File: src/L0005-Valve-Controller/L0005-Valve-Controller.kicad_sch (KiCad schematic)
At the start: 33 parts, among them J1 Jumper_NO, P1 3220-20-0200-00, P14 647676-3, P15 647676-3, P16 647676-2, P2 140-504-415-000, P9 647676-2, U2 LMS8117AMP-3.3_NOPB, U5 Optocoupler

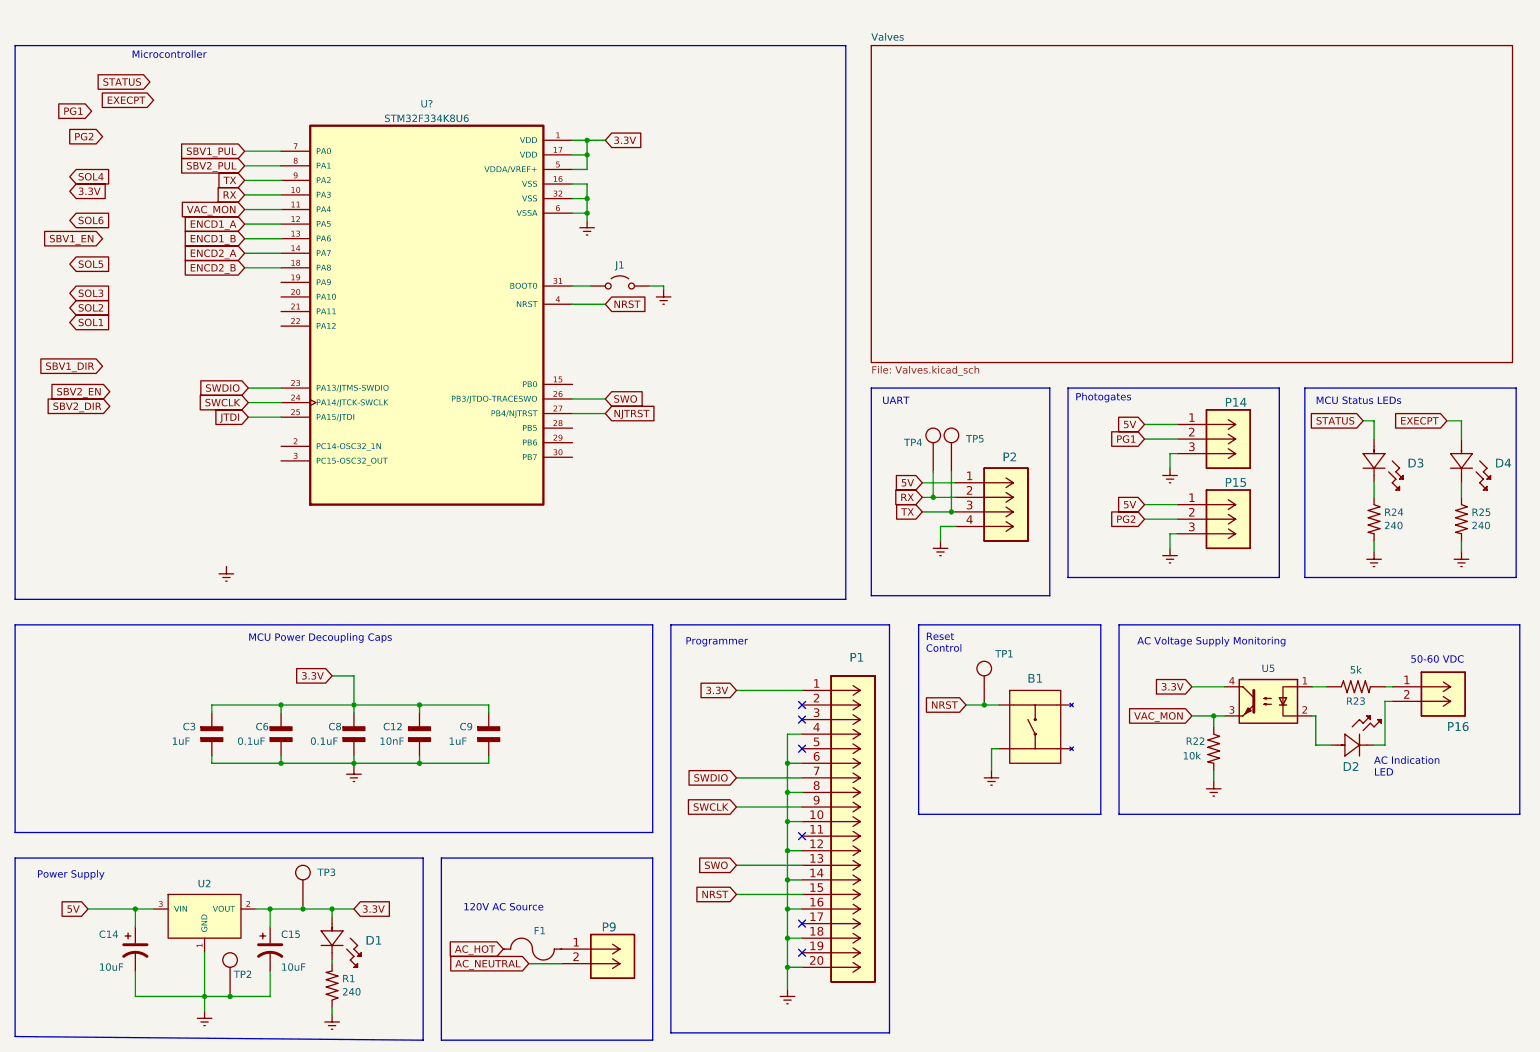
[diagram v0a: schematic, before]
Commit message: added solenoid control decoder
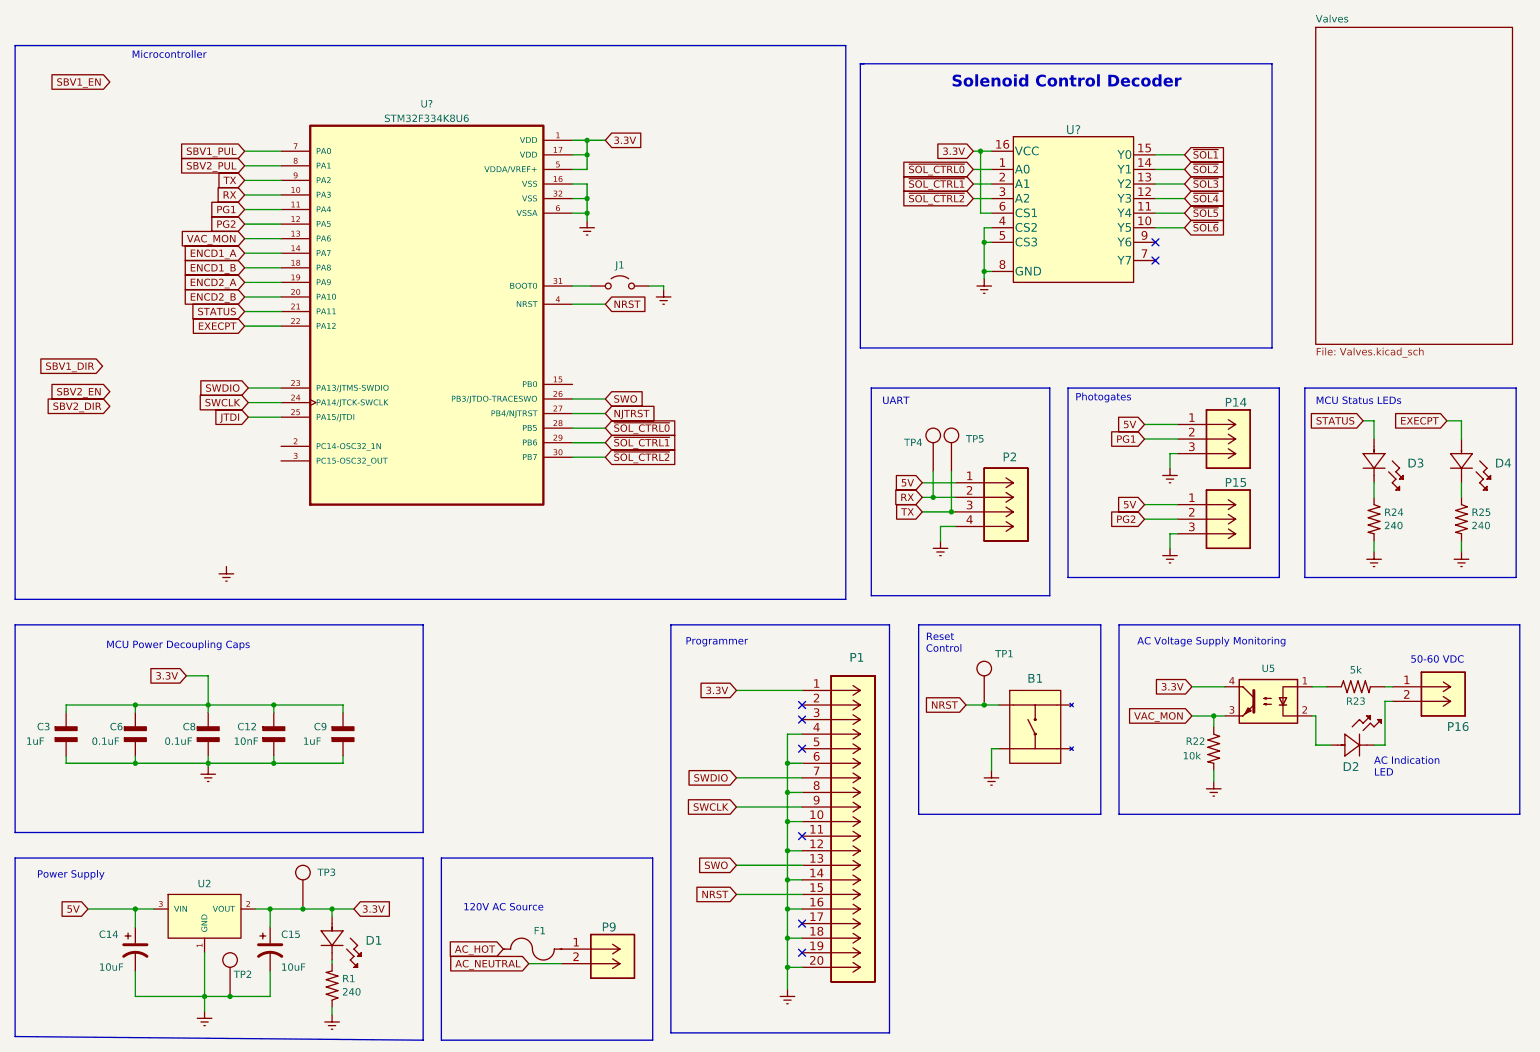
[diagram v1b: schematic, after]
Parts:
- added U?: MC74HCT138ADR2G, SOIC-16_ONS, symbol L0005-Valve-Controller:MC74HCT138ADR2G
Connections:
- net 3.3V: now also U?.16 (VCC), U?.6 (CS1)
- net ENCD1_A: now also U?.14 (PA7); no longer U?.12 (PA5)
- net ENCD1_B: now also U?.18 (PA8); no longer U?.13 (PA6)
- net ENCD2_A: now also U?.19 (PA9); no longer U?.14 (PA7)
- net ENCD2_B: now also U?.20 (PA10); no longer U?.18 (PA8)
- net EXECPT: now also U?.22 (PA12)
- net Earth: now also U?.4 (CS2), U?.5 (CS3), U?.8 (GND)
- net PG1: now also U?.11 (PA4)
- net PG2: now also U?.12 (PA5)
- net STATUS: now also U?.21 (PA11)
- net VAC_MON: now also U?.13 (PA6); no longer U?.11 (PA4)
- net ~{SOL_CTRL0}: now reaches U?.28 (PB5)
- net ~{SOL_CTRL0}: now also U?.1 (A0)
- net ~{SOL_CTRL1}: now reaches U?.29 (PB6)
- net ~{SOL_CTRL1}: now also U?.2 (A1)
- net ~{SOL_CTRL2}: now reaches U?.30 (PB7)
- net ~{SOL_CTRL2}: now also U?.3 (A2)
- new net ~{SOL1}: U?.15 (Y0)
- new net ~{SOL2}: U?.14 (Y1)
- new net ~{SOL3}: U?.13 (Y2)
- new net ~{SOL4}: U?.12 (Y3)
- new net ~{SOL5}: U?.11 (Y4)
- new net ~{SOL6}: U?.10 (Y5)
- no-connect marks 6 -> 8
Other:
- note added: "Solenoid Control Decoder"
- moved on the sheet: C12, C3, C6, C8, C9

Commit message: added STM32H7 MCU
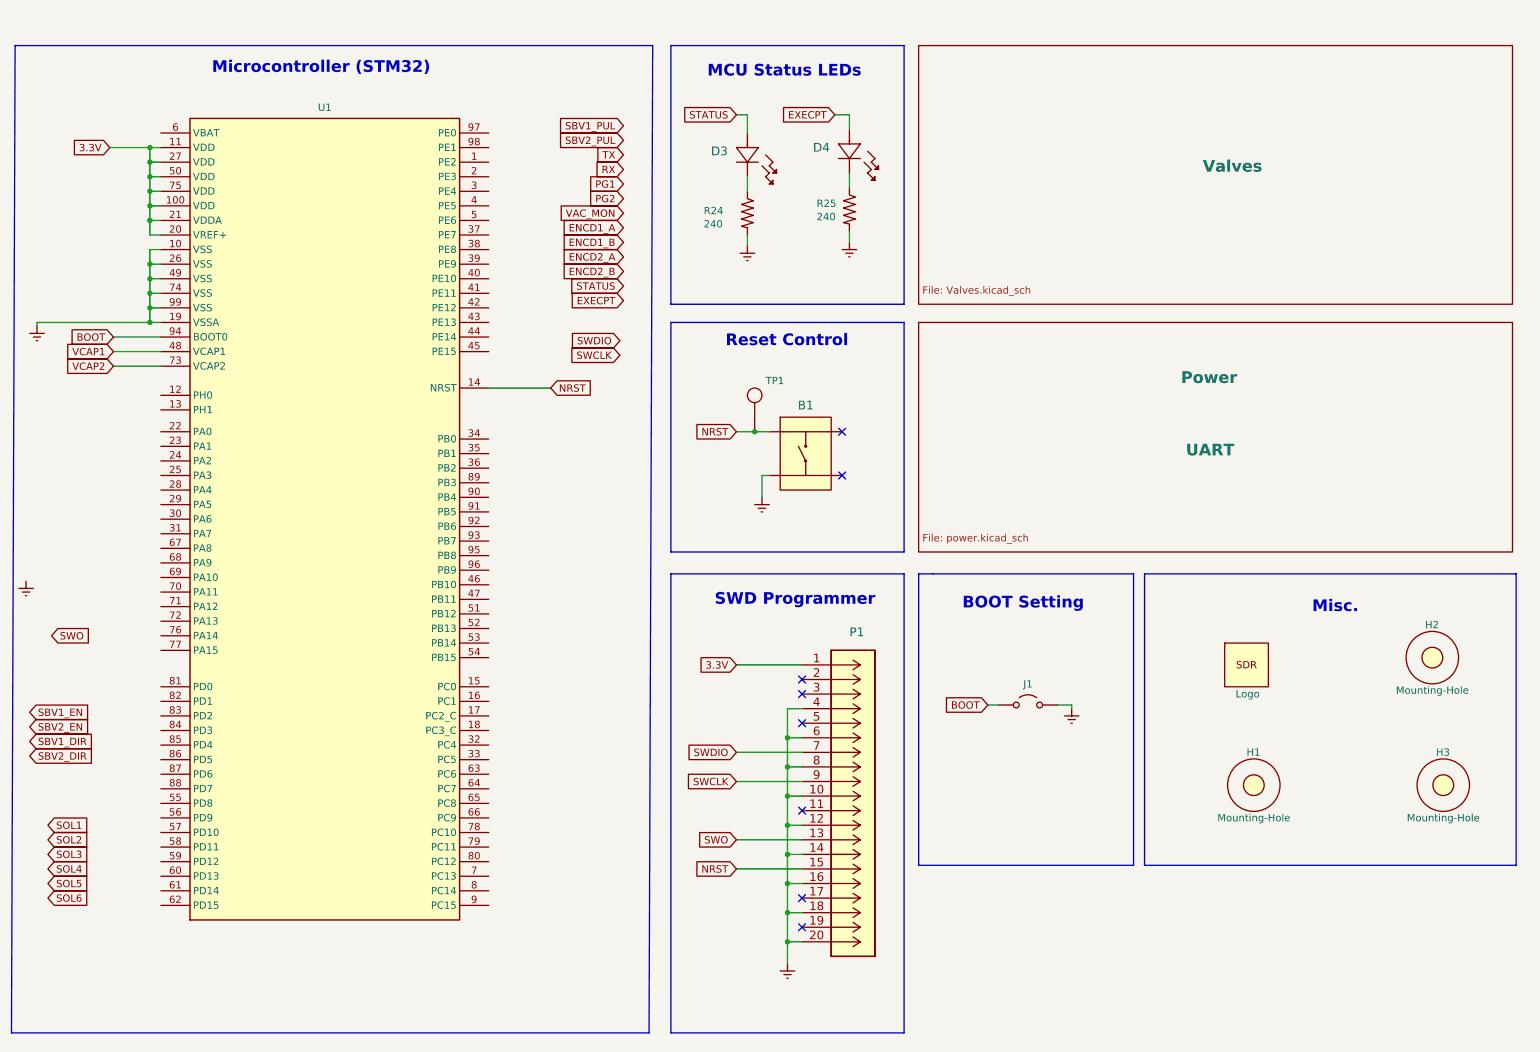
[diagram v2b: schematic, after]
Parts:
- removed C12: 10nF, L0005-Valve-Controller:CAP_0603, symbol L0005-Valve-Controller:CAP_0603
- removed C14, C15: 10uF, L0005-Valve-Controller:T491A106K010AT, symbol L0005-Valve-Controller:CAP_Polar
- removed C3, C9: 1uF, L0005-Valve-Controller:CAP_0603, symbol L0005-Valve-Controller:CAP_0603
- removed C6, C8: 0.1uF, L0005-Valve-Controller:CAP_0603, symbol L0005-Valve-Controller:CAP_0603
- removed D1, D2: LED_GREEN, L0005-Valve-Controller:SML-LX1206GC-TR, symbol L0005-Valve-Controller:LED_GREEN
- removed F1: 0678L9100-02, L0005-Valve-Controller:FUSC9830X318N, symbol L0005-Valve-Controller:0678L9100-02
- removed P14, P15: 647676-3, L0005-Valve-Controller:647676-3, symbol L0005-Valve-Controller:647676-3
- removed P16, P9: 647676-2, L0005-Valve-Controller:TE_647676-2, symbol L0005-Valve-Controller:647676-2
- removed P2: 140-504-415-000, L0005-Valve-Controller:140-504-415-000, symbol L0005-Valve-Controller:140-504-415-000
- removed R1: 240, L0005-Valve-Controller:RES_0603, symbol L0005-Valve-Controller:RES_0603
- removed R22: 10k, L0005-Valve-Controller:RES_0603, symbol L0005-Valve-Controller:RES_0603
- removed R23: 5k, L0005-Valve-Controller:RES_0603, symbol Engine-Controller:RES_0805
- removed TP2, TP3, TP4, TP5: TP, L0005-Valve-Controller:TP, symbol L0005-Valve-Controller:TP
- removed U2: LMS8117AMP-3.3_NOPB, L0005-Valve-Controller:LMS8117AMP-3.3NOPB, symbol L0005-Valve-Controller:LMS8117AMP-3.3_NOPB
- removed U5: Optocoupler, L0005-Valve-Controller:Opto_140105146000, symbol L0005-Valve-Controller:Optocoupler
- removed U?: MC74HCT138ADR2G, SOIC-16_ONS, symbol L0005-Valve-Controller:MC74HCT138ADR2G
- removed U?: STM32F334K8U6, QFN50P500X500X60-33N, symbol L0005-Valve-Controller:STM32F334K8U6
- added H1, H2, H3: Mounting-Hole, L0005-Valve-Controller:MountingHole_4.3mm_M4_DIN965, symbol L0005-Valve-Controller:Mounting-Hole
- added LOGO1: Logo, L0005-Valve-Controller:Logo, symbol L0005-Valve-Controller:Logo
- added U1: (no value), symbol L0005-Valve-Controller:STM32H750VBTx
- B1: value PTS647SM38SMTR2LFS -> (none); footprint L0005-Valve-Controller:PTS647SM38SMTR2LFS -> SW_PTS647SM38SMTR2LFS_CNK
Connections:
- net 3.3V: now also U1.100 (VDD), U1.11 (VDD), U1.20 (VREF+), U1.21 (VDDA), U1.27 (VDD), U1.50 (VDD), U1.75 (VDD)
- net Earth: now also U1.10 (VSS), U1.19 (VSSA), U1.26 (VSS), U1.49 (VSS), U1.74 (VSS), U1.99 (VSS)
- net NRST: now also U1.14 (NRST)
- net BOOT: now reaches J1.1 (A)
- net BOOT: now also U1.94 (BOOT0)
- new net VCAP1: U1.48 (VCAP1)
- new net VCAP2: U1.73 (VCAP2)
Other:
- added sheet Power (power.kicad_sch)
- note added: "BOOT Setting"
- note added: "Microcontroller (STM32)"
- note added: "Misc."
- note added: "SWD Programmer"
- note removed: "120V AC Source"
- note removed: "50-60 VDC"
- note removed: "AC Indication LED"
- note removed: "AC Voltage Supply Monitoring"
- note removed: "MCU Power Decoupling Caps"
- note removed: "Microcontroller"
- note removed: "Photogates"
- note removed: "Power Supply"
- note removed: "Programmer"
- note removed: "Solenoid Control Decoder"
- note removed: "UART"
- moved on the sheet: D3, D4, J1, P1, R24, R25, TP1

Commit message: updated schematic with STM32H7 MCU
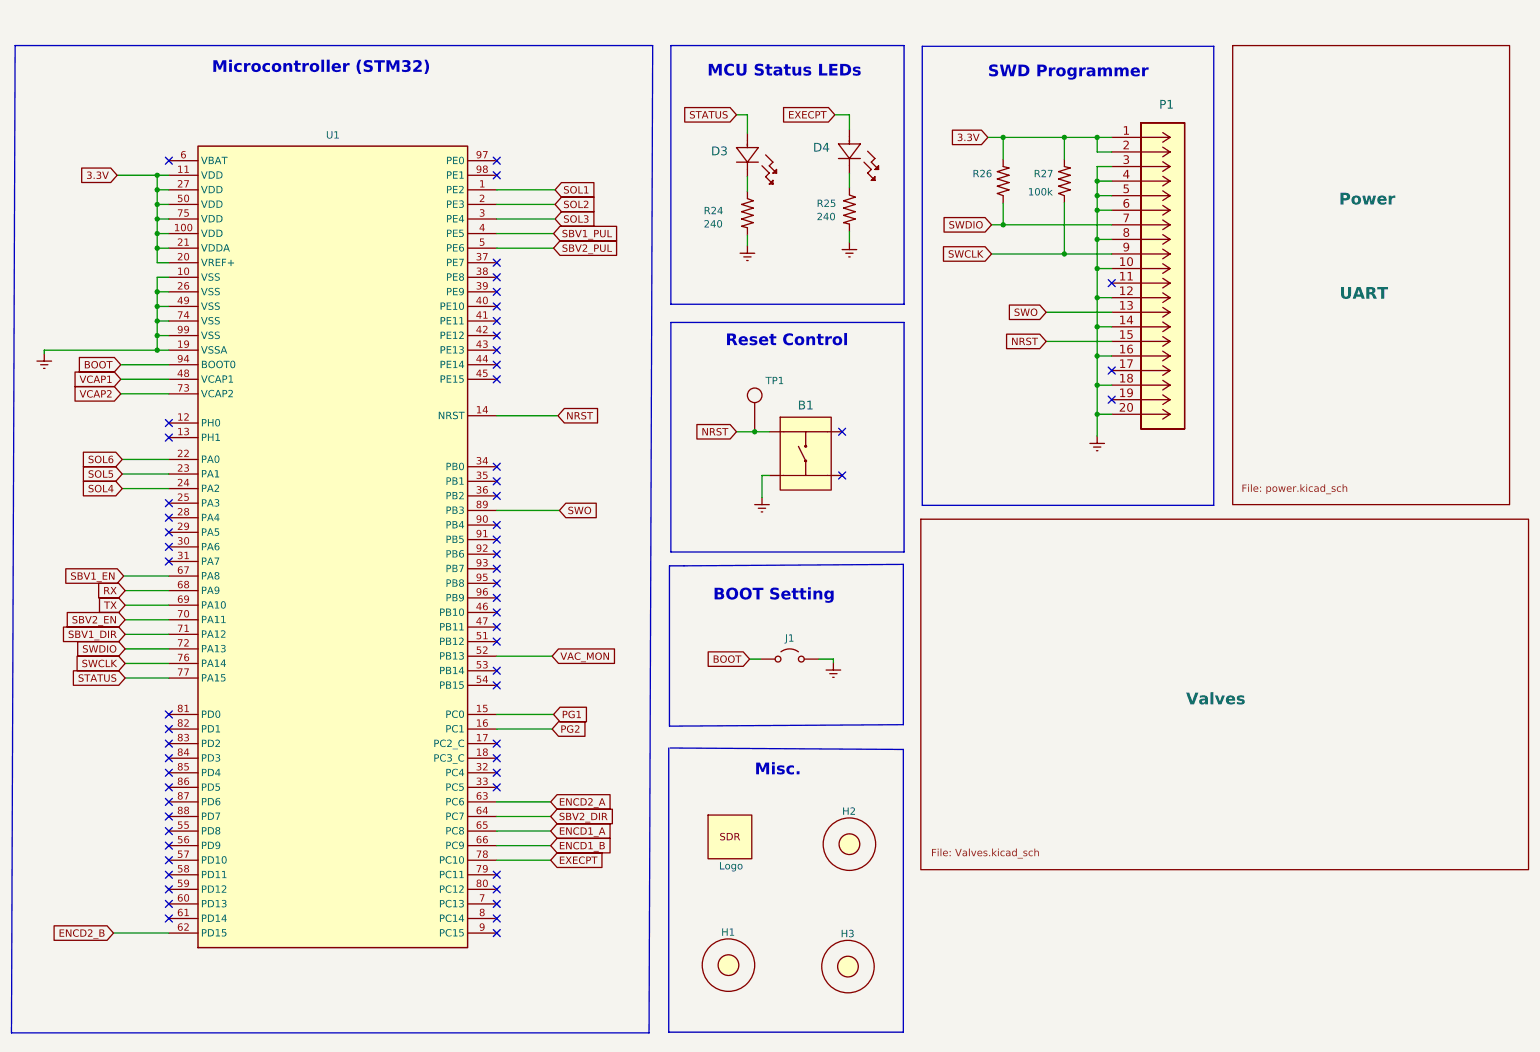
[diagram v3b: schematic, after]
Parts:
- added R26: (no value), symbol L0005-Valve-Controller:RES_0603
- added R27: 100k, symbol L0005-Valve-Controller:RES_0603
- H1, H2, H3: value Mounting-Hole -> (none); footprint L0005-Valve-Controller:MountingHole_4.3mm_M4_DIN965 -> (none)
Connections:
- net 3.3V: now also P1.2, R26.2, R27.2
- net ENCD1_A: now also U1.65 (PC8)
- net ENCD1_B: now also U1.66 (PC9)
- net ENCD2_A: now also U1.63 (PC6)
- net ENCD2_B: now also U1.62 (PD15)
- net EXECPT: now also U1.78 (PC10)
- net Earth: now also P1.3, P1.5
- net PG1: now also U1.15 (PC0)
- net PG2: now also U1.16 (PC1)
- net RX: now also U1.68 (PA9)
- net SBV1_DIR: now also U1.71 (PA12)
- net SBV1_EN: now also U1.67 (PA8)
- net SBV1_PUL: now also U1.4 (PE5)
- net SBV2_DIR: now also U1.64 (PC7)
- net SBV2_EN: now also U1.70 (PA11)
- net SBV2_PUL: now also U1.5 (PE6)
- net SOL1: now also U1.1 (PE2)
- net SOL2: now also U1.2 (PE3)
- net SOL3: now also U1.3 (PE4)
- net SOL4: now also U1.24 (PA2)
- net SOL5: now also U1.23 (PA1)
- net SOL6: now also U1.22 (PA0)
- net STATUS: now also U1.77 (PA15)
- net SWCLK: now also U1.76 (PA14), R27.1
- net SWDIO: now also U1.72 (PA13), R26.1
- net SWO: now also U1.89 (PB3)
- net TX: now also U1.69 (PA10)
- net VAC_MON: now also U1.52 (PB13)
- no-connect marks 8 -> 62
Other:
- moved on the sheet: H1, H2, H3, J1, P1, U1

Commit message: plotted schematic to pdf
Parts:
- added C15: (no value), symbol L0005-Valve-Controller:CAP_0603
- B1: value (none) -> PTS647SM38SMTR2LFS; footprint SW_PTS647SM38SMTR2LFS_CNK -> (none)
- H1, H2, H3: value (none) -> Mounting-Hole; footprint (none) -> L0005-Valve-Controller:MountingHole_4.3mm_M4_DIN965
- R26: value (none) -> 100k
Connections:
- net Earth: now also C15.2
- net NRST: now also C15.1
- net SOL4: now also U1.22 (PA0); no longer U1.24 (PA2)
- net SOL6: now also U1.24 (PA2); no longer U1.22 (PA0)
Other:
- moved on the sheet: U1
